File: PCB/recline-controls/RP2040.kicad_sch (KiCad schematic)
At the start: 27 parts, among them J1 DX07S016JA1R1500, J2 Conn_01x03, SW1 TL3330AF260QG, SW2 TL3330AF260QG, U1 TEMPLATE, U2 RP2040, X1 ABM8G-12.000MHZ-18-D2Y-T

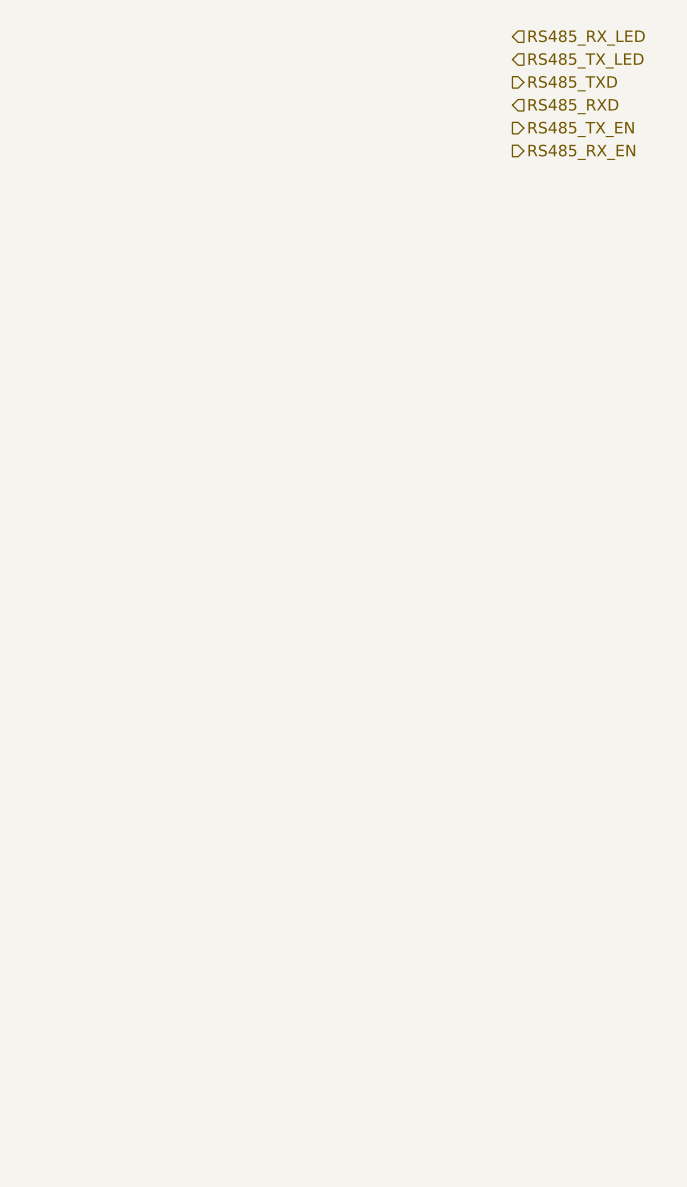
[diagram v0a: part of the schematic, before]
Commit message: Recline Controls
Recline Control board and human machine interface board schematic complete !
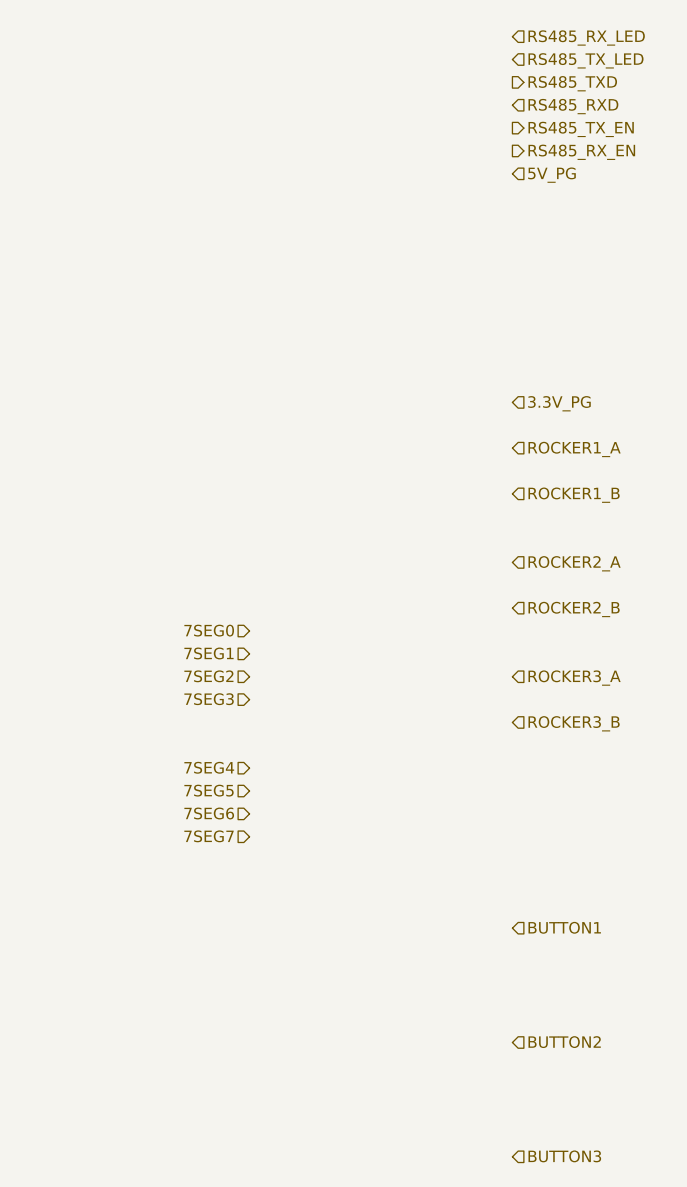
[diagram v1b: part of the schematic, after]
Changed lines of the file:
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@@
+		)
+	)
+	(hierarchical_label "7SEG1"
+		(shape input)
+		(at 224.79 119.38 180)
+		(fields_autoplaced yes)
+		(effects
+			(font
+				(size 1.27 1.27)
+			)
+			(justify right)
+		)
+	)
+	(hierarchical_label "BUTTON1"
+		(shape input)
+		(at 254 149.86 0)
+		(fields_autoplaced yes)
+		(effects
+			(font
+				(size 1.27 1.27)
+			)
+			(justify left)
+		)
+	)
+	(hierarchical_label "7SEG3"
+		(shape input)
+		(at 224.79 124.46 180)
+		(fields_autoplaced yes)
+		(effects
+			(font
+				(size 1.27 1.27)
+			)
+			(justify right)
+		)
+	)
+	(hierarchical_label "ROCKER3_A"
+		(shape input)
+		(at 254 121.92 0)
+		(fields_autoplaced yes)
+		(effects
+			(font
+				(size 1.27 1.27)
+			)
+			(justify left)
+		)
+	)
+	(hierarchical_label "5V_PG"
+		(shape input)
+		(at 254 66.04 0)
+		(fields_autoplaced yes)
+		(effects
+			(font
+				(size 1.27 1.27)
+			)
+			(justify left)
+		)
+	)
+	(hierarchical_label "7SEG6"
+		(shape input)
+		(at 224.79 137.16 180)
+		(fields_autoplaced yes)
+		(effects
+			(font
+				(size 1.27 1.27)
+			)
+			(justify right)
 		)
 	)
@@
 		)
 	)
+	(hierarchical_label "7SEG4"
+		(shape input)
+		(at 224.79 132.08 180)
+		(fields_autoplaced yes)
+		(effects
+			(font
+				(size 1.27 1.27)
+			)
+			(justify right)
+		)
+	)
+	(hierarchical_label "ROCKER2_A"
+		(shape input)
+		(at 254 109.22 0)
+		(fields_autoplaced yes)
+		(effects
+			(font
+				(size 1.27 1.27)
+			)
+			(justify left)
+		)
+	)
 	(hierarchical_label "RS485_TX_LED"
 		(shape input)
 		(at 254 53.34 0)
+		(fields_autoplaced yes)
+		(effects
+			(font
+				(size 1.27 1.27)
+			)
+			(justify left)
+		)
+	)
+	(hierarchical_label "ROCKER1_A"
+		(shape input)
+		(at 254 96.52 0)
 		(fields_autoplaced yes)
 		(effects
@@
 		)
 	)
+	(hierarchical_label "7SEG0"
+		(shape input)
+		(at 224.79 116.84 180)
+		(fields_autoplaced yes)
+		(effects
+			(font
+				(size 1.27 1.27)
+			)
+			(justify right)
+		)
+	)
+	(hierarchical_label "7SEG5"
+		(shape input)
+		(at 224.79 134.62 180)
+		(fields_autoplaced yes)
+		(effects
+			(font
+				(size 1.27 1.27)
+			)
+			(justify right)
+		)
+	)
+	(hierarchical_label "BUTTON3"
+		(shape input)
+		(at 254 175.26 0)
+		(fields_autoplaced yes)
+		(effects
+			(font
+				(size 1.27 1.27)
+			)
+			(justify left)
+		)
+	)
 	(hierarchical_label "RS485_TX_EN"
 		(shape output)
@@
 		)
 	)
+	(hierarchical_label "7SEG2"
+		(shape input)
+		(at 224.79 121.92 180)
+		(fields_autoplaced yes)
+		(effects
+			(font
+				(size 1.27 1.27)
+			)
+			(justify right)
+		)
+	)
+	(hierarchical_label "ROCKER2_B"
+		(shape input)
+		(at 254 114.3 0)
+		(fields_autoplaced yes)
+		(effects
+			(font
+				(size 1.27 1.27)
+			)
+			(justify left)
+		)
+	)
 	(hierarchical_label "RS485_RX_EN"
 		(shape output)
@@
 		(fields_autoplaced yes)
 		(effects
+			(font
+				(size 1.27 1.27)
+			)
+			(justify left)
+		)
+	)
+	(hierarchical_label "ROCKER3_B"
+		(shape input)
+		(at 254 127 0)
+		(fields_autoplaced yes)
+		(effects
+			(font
+				(size 1.27 1.27)
+			)
+			(justify left)
+		)
+	)
+	(hierarchical_label "ROCKER1_B"
+		(shape input)
+		(at 254 101.6 0)
+		(fields_autoplaced yes)
+		(effects
+			(font
+				(size 1.27 1.27)
+			)
+			(justify left)
+		)
+	)
+	(hierarchical_label "3.3V_PG"
+		(shape input)
+		(at 254 91.44 0)
+		(fields_autoplaced yes)
+		(effects
+			(font
+				(size 1.27 1.27)
+			)
+			(justify left)
+		)
+	)
+	(hierarchical_label "7SEG7"
+		(shape input)
+		(at 224.79 139.7 180)
+		(fields_autoplaced yes)
+		(effects
+			(font
+				(size 1.27 1.27)
+			)
+			(justify right)
+		)
+	)
+	(hierarchical_label "BUTTON2"
+		(shape input)
+		(at 254 162.56 0)
+		(fields_autoplaced yes)
+		(effects

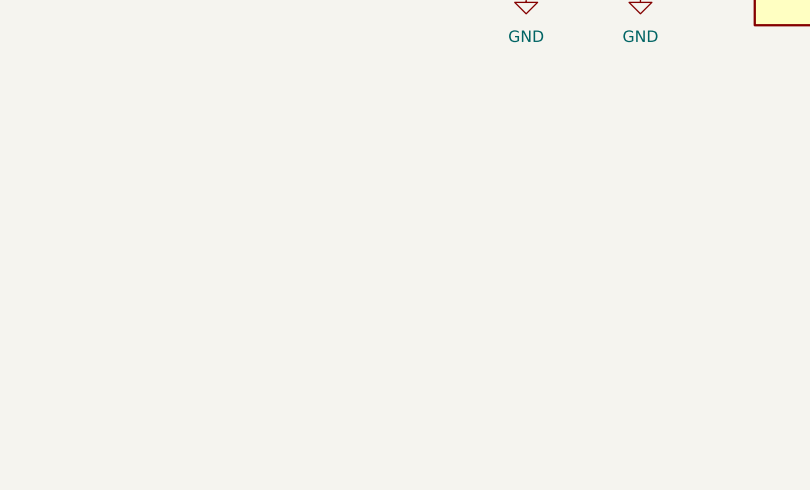
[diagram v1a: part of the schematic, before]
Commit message: PCB Started
PCB design for Recline Control Board started, figuring out PCB shape and connector positioning, work in progress !
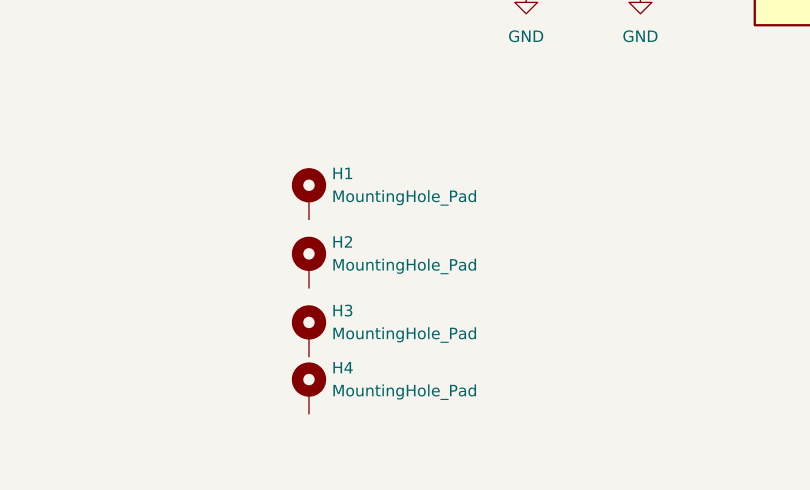
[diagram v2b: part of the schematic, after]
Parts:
- added H1, H2, H3, H4: MountingHole_Pad, AVR-KiCAD-Lib-Holes_Fasteners:RPI_HAT_HOLE, symbol Mechanical:MountingHole_Pad
- C2, C4: footprint growbox-KiCAD-Capacitors:C0402 -> AVR-KiCAD-Lib-Capacitors:C0402
- J2: footprint (none) -> AVR-KiCAD-Lib-Connectors:Pin_Header_Angled_1x03_Pitch2.54mm

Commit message: All Hardware Tweaked / 3D Renders
PCBs for Actuator Control, Recline Control HID, and 7 Segment carrier are all complete with full 3D models rendering. 3D Renders of all board added to repository img directory.
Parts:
- removed R4, R5: RC1206FR-075K1L, AVR-KiCAD-Lib-Resistors:R1206, symbol AVR-KiCAD-Lib-Resistors:RC1206FR-075K1L
- added R4, R5: RC0402FR-075K1L, AVR-KiCAD-Lib-Resistors:R0402, symbol AVR-KiCAD-Lib-Resistors:RC0402FR-075K1L
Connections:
- net 3.3V_PG: now also U2.16 (GPIO13)
- net 5V_PG: now also U2.15 (GPIO12)
- net 7SEG0: now also U2.34 (GPIO22)
- net 7SEG1: now also U2.35 (GPIO23)
- net 7SEG2: now also U2.36 (GPIO24)
- net 7SEG3: now also U2.37 (GPIO25)
- net 7SEG4: now also U2.38 (GPIO26_ADC0)
- net 7SEG5: now also U2.39 (GPIO27_ADC1)
- net 7SEG6: now also U2.40 (GPIO28_ADC2)
- net 7SEG7: now also U2.41 (GPIO29_ADC3)
- net BUTTON1: now also U2.12 (GPIO9)
- net BUTTON2: now also U2.11 (GPIO8)
- net BUTTON3: now also U2.8 (GPIO6)
- net GND: now also R4.2, R5.2
- net ROCKER1_A: now also U2.7 (GPIO5)
- net ROCKER1_B: now also U2.6 (GPIO4)
- net ROCKER2_A: now also U2.5 (GPIO3)
- net ROCKER2_B: now also U2.4 (GPIO2)
- net ROCKER3_A: now also U2.3 (GPIO1)
- net ROCKER3_B: now also U2.2 (GPIO0)
- net RS485_RXD: now also U2.28 (GPIO17)
- net RS485_RX_EN: now also U2.30 (GPIO19)
- net RS485_RX_LED: now also U2.31 (GPIO20)
- net RS485_TXD: now also U2.27 (GPIO16)
- net RS485_TX_EN: now also U2.29 (GPIO18)
- net RS485_TX_LED: now also U2.32 (GPIO21)
- net AUXBUTTON: now reaches U2.13 (GPIO10)
- net SWCLK: now reaches J2.1 (Pin_1), U2.24 (SWCLK)
- net SWD: now reaches J2.3 (Pin_3), U2.25 (SWD)
- net at J1.3 (CC1): now also R5.1
- net at J1.9 (CC2): now also R4.1
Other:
- note added: "RP2040 - MCU"
- moved on the sheet: C1, C10, C11, C12, C13, C14, C2, C3, C4, C5, C6, C7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

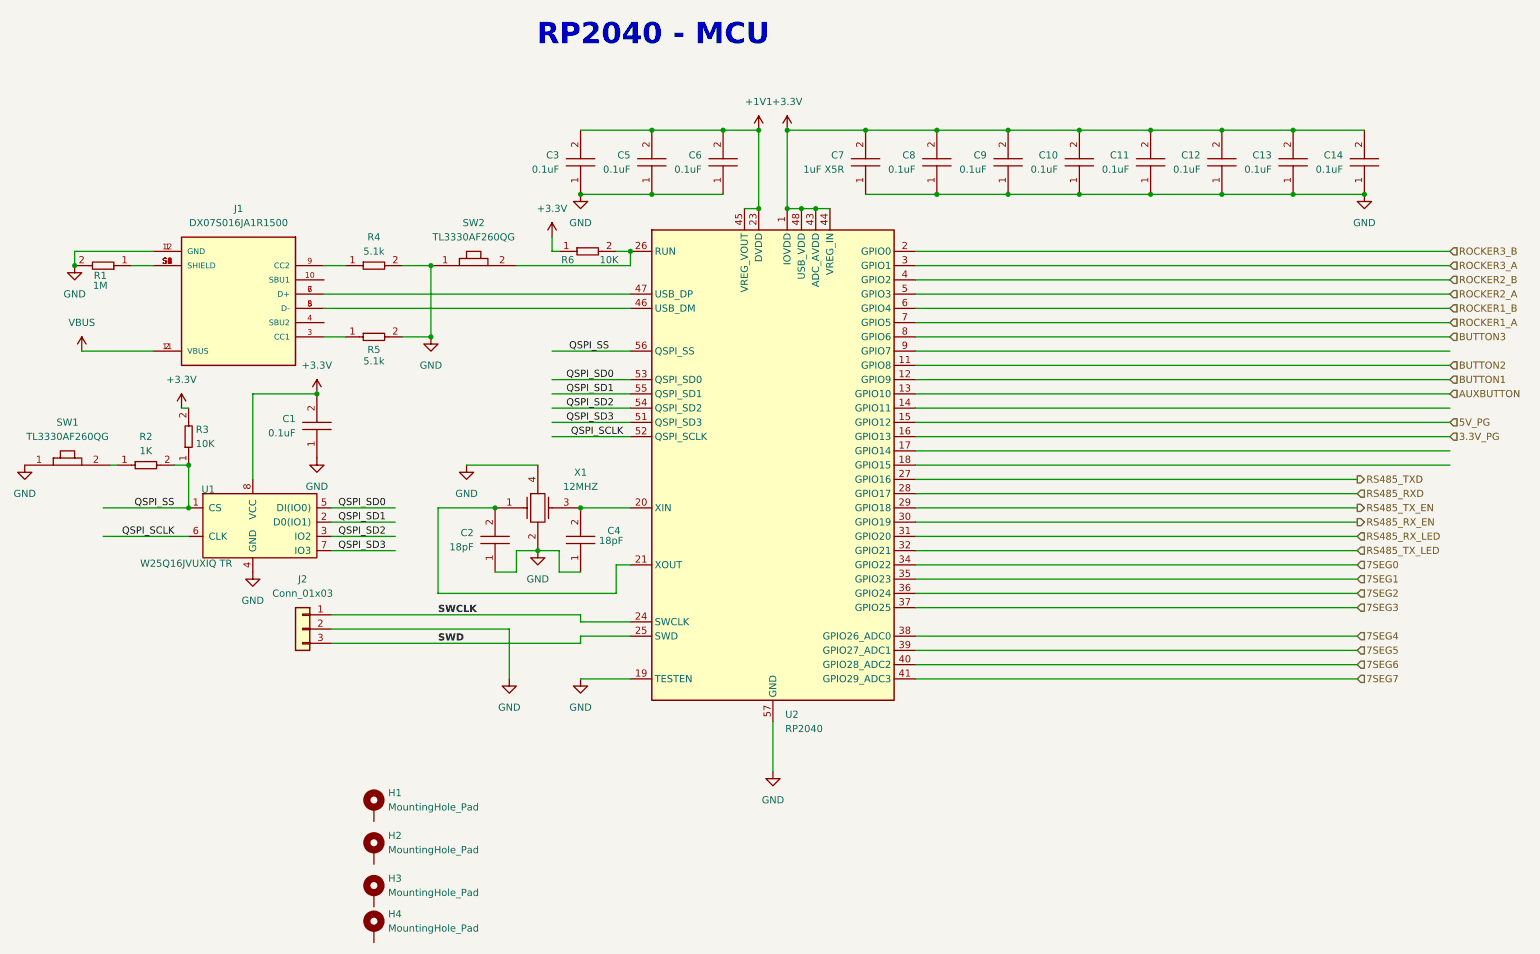
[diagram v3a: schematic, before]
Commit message: HID
Changes made to recline control HID board. Power input section redesigned, 5V regulator removed, RS485 circuit updated with fixes that other boards received. Redesign or internal plane topology following changes to RS485 section. Via stitching all around.
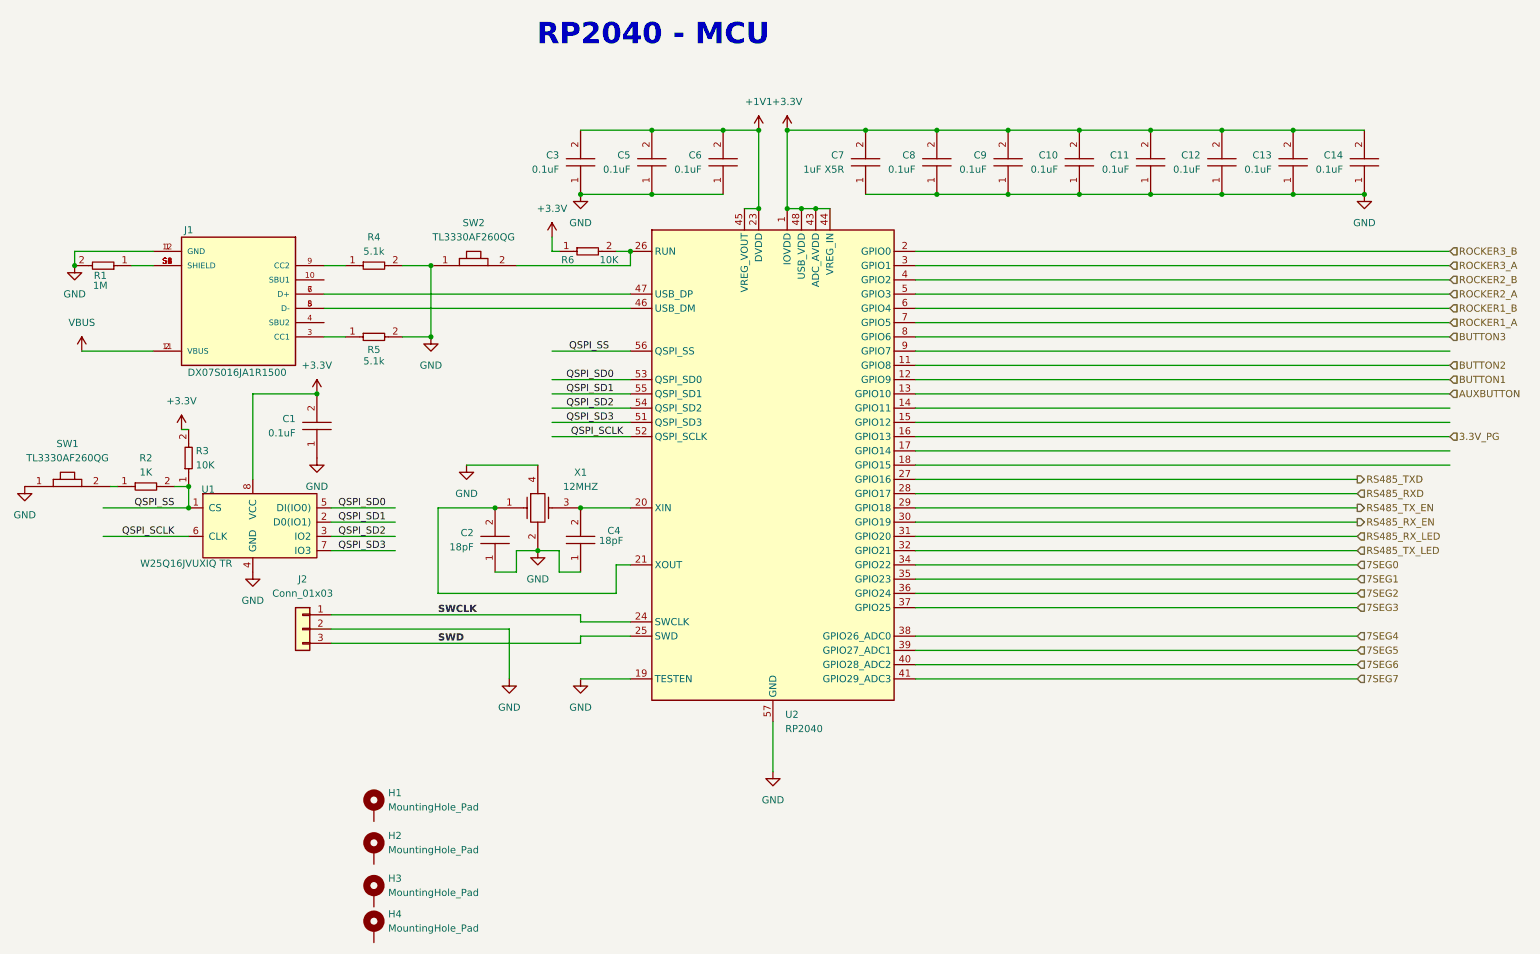
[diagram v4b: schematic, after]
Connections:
- net 5V_PG: no longer names the net of U2.15 (GPIO12)
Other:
- moved on the sheet: R2, R3, SW1
